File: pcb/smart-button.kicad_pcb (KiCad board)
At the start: 2 copper layers, 62.3 x 33 mm, 5 parts, among them J1 Conn_01x15, J2 Conn_01x15, SW1 SW_Push, SW2 SW_Push, SW3 SW_Push

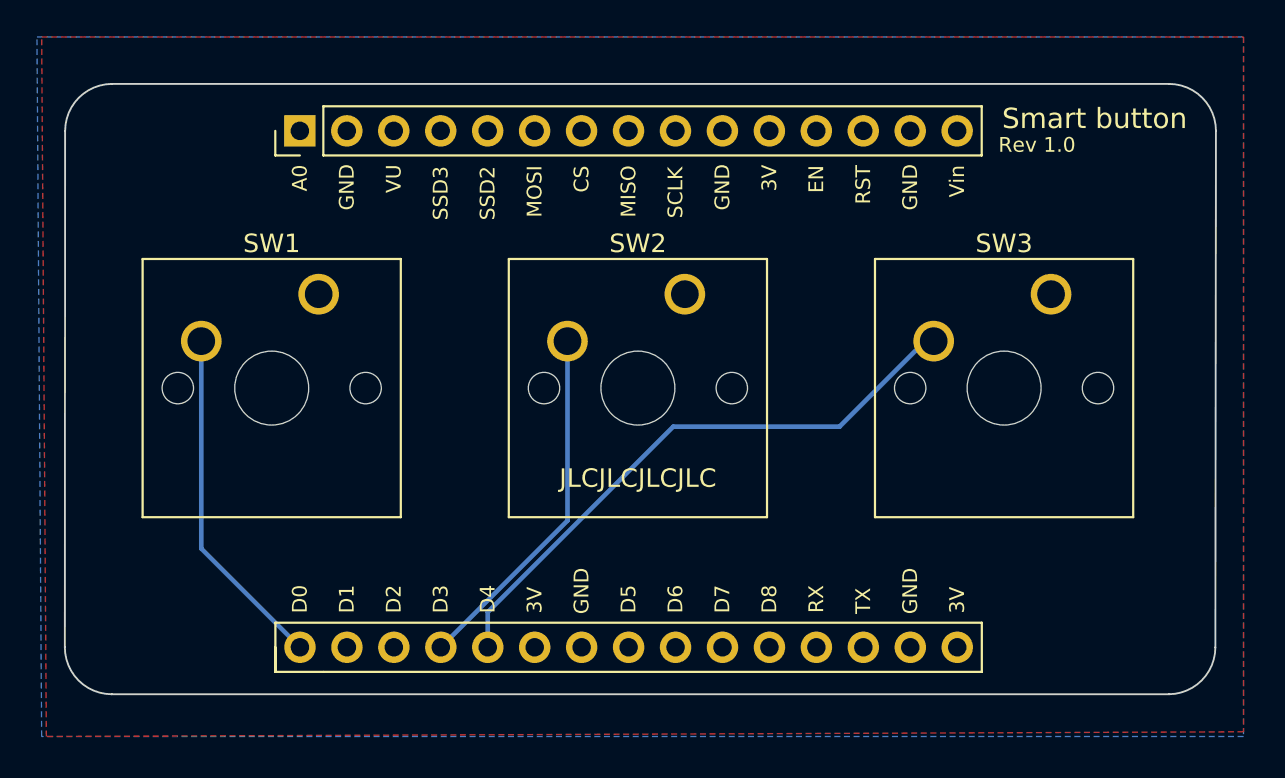
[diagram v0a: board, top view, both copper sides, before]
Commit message: Using simple pins not connected to leds and verified internal pull-up resistors
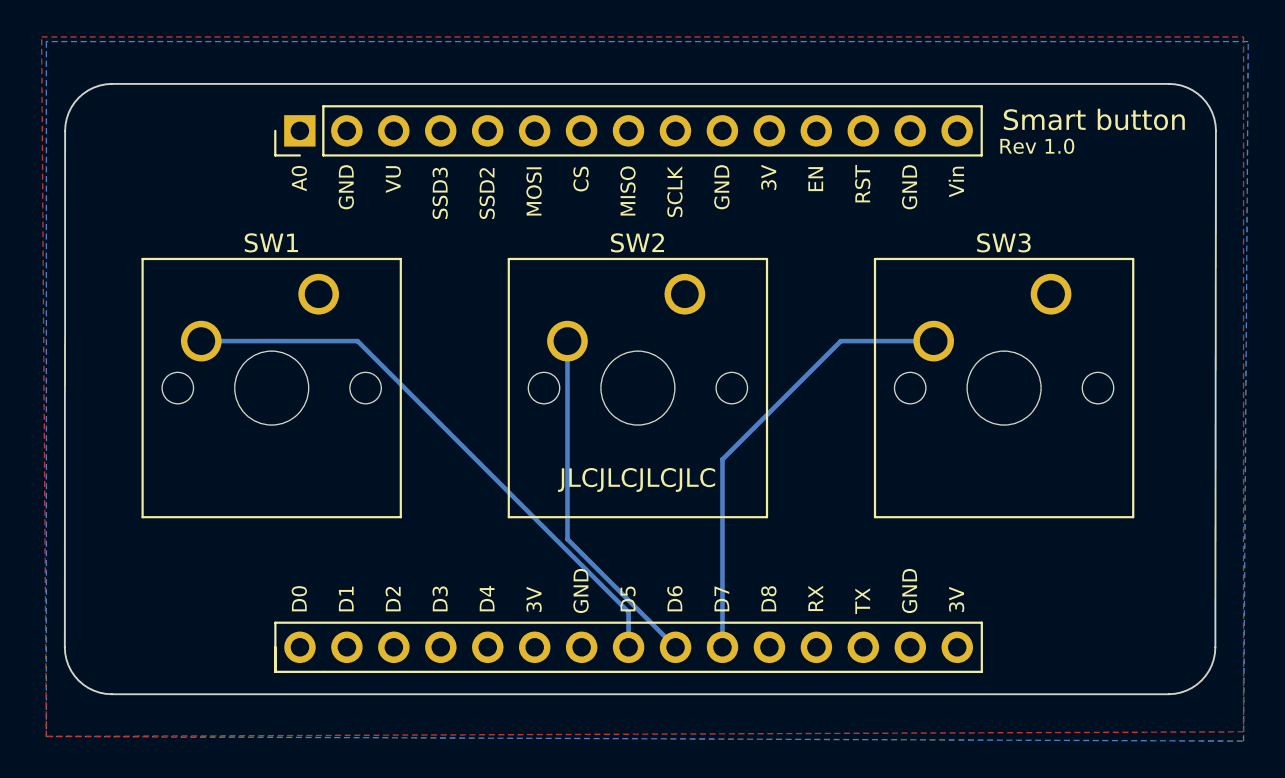
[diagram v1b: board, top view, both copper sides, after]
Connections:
- J2 pad 1: Net-(J2-Pad1) -> unconnected-(J2-Pad1)
- J2 pad 10: unconnected-(J2-Pad10) -> Net-(J2-Pad10)
- J2 pad 4: Net-(J2-Pad4) -> unconnected-(J2-Pad4)
- J2 pad 5: Net-(J2-Pad5) -> unconnected-(J2-Pad5)
- J2 pad 8: unconnected-(J2-Pad8) -> Net-(J2-Pad8)
- J2 pad 9: unconnected-(J2-Pad9) -> Net-(J2-Pad9)
- SW1 pad 2: Net-(J2-Pad1) -> Net-(J2-Pad8)
- SW2 pad 2: Net-(J2-Pad4) -> Net-(J2-Pad9)
- SW3 pad 2: Net-(J2-Pad5) -> Net-(J2-Pad10)
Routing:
- net Net-(J2-Pad5): track 32.1 -> 0.00 mm
- net Net-(J2-Pad8): track 0.00 -> 31.1 mm
- net Net-(J2-Pad10): track 0.00 -> 24.2 mm
- net Net-(J2-Pad4): track 19.4 -> 0.00 mm
- net Net-(J2-Pad9): track 0.00 -> 19.0 mm
- net Net-(J2-Pad1): track 18.8 -> 0.00 mm
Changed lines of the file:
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@@
     (32 "B.Adhes" user "B.Adhesive")
     (33 "F.Adhes" user "F.Adhesive")
-    (34 "B.Paste" user "B.Plakken")
-    (35 "F.Paste" user "F.Plakken")
     (36 "B.SilkS" user "B.Silkscreen")
     (37 "F.SilkS" user "F.Silkscreen")
@@
   )
   (setup
+    (stackup
+      (layer "F.SilkS" (type "Top Silk Screen"))
+      (layer "F.Mask" (type "Top Solder Mask") (thickness 0.01))
+      (layer "F.Cu" (type "copper") (thickness 0.035))
+      (layer "dielectric 1" (type "core") (thickness 1.51) (material "FR4") (epsilon_r 4.5) (loss_tangent 0.02))
+      (layer "B.Cu" (type "copper") (thickness 0.035))
+      (layer "B.Mask" (type "Bottom Solder Mask") (thickness 0.01))
+      (layer "B.SilkS" (type "Bottom Silk Screen"))
+      (copper_finish "None")
+      (dielectric_constraints no)
+    )
     (pad_to_mask_clearance 0)
     (pcbplotparams
@@
   (net 11 "unconnected-(J1-Pad13)")
   (net 12 "unconnected-(J1-Pad15)")
-  (net 13 "Net-(J2-Pad1)")
+  (net 13 "unconnected-(J2-Pad1)")
   (net 14 "unconnected-(J2-Pad2)")
   (net 15 "unconnected-(J2-Pad3)")
-  (net 16 "Net-(J2-Pad4)")
-  (net 17 "Net-(J2-Pad5)")
+  (net 16 "unconnected-(J2-Pad4)")
+  (net 17 "unconnected-(J2-Pad5)")
   (net 18 "unconnected-(J2-Pad6)")
-  (net 19 "unconnected-(J2-Pad8)")
-  (net 20 "unconnected-(J2-Pad9)")
-  (net 21 "unconnected-(J2-Pad10)")
+  (net 19 "Net-(J2-Pad8)")
+  (net 20 "Net-(J2-Pad9)")
+  (net 21 "Net-(J2-Pad10)")
   (net 22 "unconnected-(J2-Pad11)")
   (net 23 "unconnected-(J2-Pad12)")
@@
       (net 2 "GND") (pinfunction "1") (pintype "passive"))
     (pad "2" thru_hole circle (at -6.35 2.54) (size 2.2 2.2) (drill 1.5) (layers *.Cu *.Mask)
-      (net 13 "Net-(J2-Pad1)") (pinfunction "2") (pintype "passive"))
+      (net 19 "Net-(J2-Pad8)") (pinfunction "2") (pintype "passive"))
     (model "${KICAD6_3DMODEL_DIR}/Button_Switch_Keyboard.3dshapes/SW_Cherry_MX_1.00u_PCB.wrl"
       (offset (xyz 0 0 0))
@@
       (net 2 "GND") (pinfunction "1") (pintype "passive"))
     (pad "2" thru_hole circle (at -6.35 2.54) (size 2.2 2.2) (drill 1.5) (layers *.Cu *.Mask)
-      (net 17 "Net-(J2-Pad5)") (pinfunction "2") (pintype "passive"))
+      (net 21 "Net-(J2-Pad10)") (pinfunction "2") (pintype "passive"))
     (model "${KICAD6_3DMODEL_DIR}/Button_Switch_Keyboard.3dshapes/SW_Cherry_MX_1.00u_PCB.wrl"
       (offset (xyz 0 0 0))
@@
     (fp_line (start -0.635 -1.27) (end 1.27 -1.27) (layer "F.Fab") (width 0.1))
     (pad "1" thru_hole circle (at 0 0 90) (size 1.7 1.7) (drill 1) (layers *.Cu *.Mask)
-      (net 13 "Net-(J2-Pad1)") (pinfunction "Pin_1") (pintype "passive"))
+      (net 13 "unconnected-(J2-Pad1)") (pinfunction "Pin_1") (pintype "passive+no_connect"))
     (pad "2" thru_hole oval (at 0 2.54 90) (size 1.7 1.7) (drill 1) (layers *.Cu *.Mask)
       (net 14 "unconnected-(J2-Pad2)") (pinfunction "Pin_2") (pintype "passive+no_connect"))
@@
       (net 15 "unconnected-(J2-Pad3)") (pinfunction "Pin_3") (pintype "passive+no_connect"))
     (pad "4" thru_hole oval (at 0 7.62 90) (size 1.7 1.7) (drill 1) (layers *.Cu *.Mask)
-      (net 16 "Net-(J2-Pad4)") (pinfunction "Pin_4") (pintype "passive"))
+      (net 16 "unconnected-(J2-Pad4)") (pinfunction "Pin_4") (pintype "passive+no_connect"))
     (pad "5" thru_hole oval (at 0 10.16 90) (size 1.7 1.7) (drill 1) (layers *.Cu *.Mask)
-      (net 17 "Net-(J2-Pad5)") (pinfunction "Pin_5") (pintype "passive"))
+      (net 17 "unconnected-(J2-Pad5)") (pinfunction "Pin_5") (pintype "passive+no_connect"))
     (pad "6" thru_hole oval (at 0 12.7 90) (size 1.7 1.7) (drill 1) (layers *.Cu *.Mask)
       (net 18 "unconnected-(J2-Pad6)") (pinfunction "Pin_6") (pintype "passive+no_connect"))
@@
       (net 2 "GND") (pinfunction "Pin_7") (pintype "passive"))
     (pad "8" thru_hole oval (at 0 17.78 90) (size 1.7 1.7) (drill 1) (layers *.Cu *.Mask)
-      (net 19 "unconnected-(J2-Pad8)") (pinfunction "Pin_8") (pintype "passive+no_connect"))
+      (net 19 "Net-(J2-Pad8)") (pinfunction "Pin_8") (pintype "passive"))
     (pad "9" thru_hole oval (at 0 20.32 90) (size 1.7 1.7) (drill 1) (layers *.Cu *.Mask)
-      (net 20 "unconnected-(J2-Pad9)") (pinfunction "Pin_9") (pintype "passive+no_connect"))
+      (net 20 "Net-(J2-Pad9)") (pinfunction "Pin_9") (pintype "passive"))
     (pad "10" thru_hole oval (at 0 22.86 90) (size 1.7 1.7) (drill 1) (layers *.Cu *.Mask)
-      (net 21 "unconnected-(J2-Pad10)") (pinfunction "Pin_10") (pintype "passive+no_connect"))
+      (net 21 "Net-(J2-Pad10)") (pinfunction "Pin_10") (pintype "passive"))
     (pad "11" thru_hole oval (at 0 25.4 90) (size 1.7 1.7) (drill 1) (layers *.Cu *.Mask)
       (net 22 "unconnected-(J2-Pad11)") (pinfunction "Pin_11") (pintype "passive+no_connect"))
@@
       (net 2 "GND") (pinfunction "1") (pintype "passive"))
     (pad "2" thru_hole circle (at -6.35 2.54) (size 2.2 2.2) (drill 1.5) (layers *.Cu *.Mask)
-      (net 16 "Net-(J2-Pad4)") (pinfunction "2") (pintype "passive"))
+      (net 20 "Net-(J2-Pad9)") (pinfunction "2") (pintype "passive"))
     (model "${KICAD6_3DMODEL_DIR}/Button_Switch_Keyboard.3dshapes/SW_Cherry_MX_1.00u_PCB.wrl"
       (offset (xyz 0 0 0))
@@
     (effects (font (size 0.8 0.8) (thickness 0.15)) (justify mirror))
   )
-  (gr_text "Martijn\nCasteel" (at 94.742 105.41 180) (layer "B.SilkS")
+  (gr_text "Martijn\nCasteel" (at 94.612 105.41 180) (layer "B.SilkS")
     (effects (font (size 1 1) (thickness 0.15)) (justify left mirror))
   )
-  (gr_text "Shield for NodeMCU v3 (lolin) \nwith 3 CherryMX buttons." (at 56.388 124.714 180) (layer "B.SilkS")
+  (gr_text "Shield for NodeMCU v3 (lolin) \nwith 3 CherryMX buttons." (at 54.102 124.714 180) (layer "B.SilkS")
     (effects (font (size 1 1) (thickness 0.15)) (justify left mirror))
   )
@@
     (effects (font (size 0.8 0.8) (thickness 0.15)))
   )
-  (gr_text "Smart button" (at 100.146 104.748) (layer "F.SilkS")
+  (gr_text "Smart button" (at 100.146 104.848) (layer "F.SilkS")
     (effects (font (size 1.1 1.1) (thickness 0.15)))
   )
@@
     (effects (font (size 0.8 0.8) (thickness 0.15)))
   )
-  (gr_text "Rev 1.0" (at 97.028 106.172) (layer "F.SilkS")
+  (gr_text "Rev 1.0" (at 97.028 106.272) (layer "F.SilkS")
     (effects (font (size 0.8 0.8) (thickness 0.15)))
   )
@@
     (effects (font (size 0.8 0.8) (thickness 0.15)))
   )
-  (segment (start 51.816 116.786) (end 51.816 128.011) (width 0.25) (layer "B.Cu") (net 13))
-  (segment (start 51.816 128.011) (end 57.155 133.35) (width 0.25) (layer "B.Cu") (net 13))
-  (segment (start 64.775 133.35) (end 71.628 126.497) (width 0.25) (layer "B.Cu") (net 16))
-  (segment (start 71.628 126.497) (end 71.628 116.786) (width 0.25) (layer "B.Cu") (net 16))
-  (segment (start 67.315 131.445718) (end 77.348718 121.412) (width 0.25) (layer "B.Cu") (net 17))
-  (segment (start 67.315 133.35) (end 67.315 131.445718) (width 0.25) (layer "B.Cu") (net 17))
-  (segment (start 77.348718 121.412) (end 86.352265 121.412) (width 0.25) (layer "B.Cu") (net 17))
-  (segment (start 86.352265 121.412) (end 90.978265 116.786) (width 0.25) (layer "B.Cu") (net 17))
-  (segment (start 90.978265 116.786) (end 91.44 116.786) (width 0.25) (layer "B.Cu") (net 17))
+  (dimension (type aligned) (layer "B.SilkS")
+    (pts (xy 54.61 133.35) (xy 54.61 105.41))
+    (height -1.016)
+    (gr_text "27.9400 mm" (at 52.444 119.38 90) (layer "B.SilkS")
+      (effects (font (size 1 1) (thickness 0.15)) (justify left mirror))
+    )
+    (format (units 3) (units_format 1) (precision 4))
+    (style (thickness 0.15) (arrow_length 1.27) (text_position_mode 0) (extension_height 0.58642) (extension_offset 0.5) keep_text_aligned)
+  )
+  (segment (start 74.935 133.35) (end 74.935 131.445718) (width 0.25) (layer "B.Cu") (net 19))
+  (segment (start 60.275282 116.786) (end 51.816 116.786) (width 0.25) (layer "B.Cu") (net 19))
+  (segment (start 74.935 131.445718) (end 60.275282 116.786) (width 0.25) (layer "B.Cu") (net 19))
+  (segment (start 77.475 133.35) (end 71.628 127.503) (width 0.25) (layer "B.Cu") (net 20))
+  (segment (start 71.628 127.503) (end 71.628 116.786) (width 0.25) (layer "B.Cu") (net 20))
+  (segment (start 80.015 123.185) (end 86.414 116.786) (width 0.25) (layer "B.Cu") (net 21))
+  (segment (start 86.414 116.786) (end 91.44 116.786) (width 0.25) (layer "B.Cu") (net 21))
+  (segment (start 80.015 133.35) (end 80.015 123.185) (width 0.25) (layer "B.Cu") (net 21))
   (zone (net 2) (net_name "GND") (layer "F.Cu") (hatch edge 0.508)
     (connect_pads (clearance 0.508))
@@
     (polygon
       (pts
-        (xy 108.204 138.176)
-        (xy 43.18 138.176)
-        (xy 42.926 100.33)
-        (xy 108.204 100.33)
+        (xy 43.434 100.580016)
+        (xy 43.434 138.172016)
+        (xy 108.204 138.426016)
+        (xy 108.458 100.580016)
       )
     )
